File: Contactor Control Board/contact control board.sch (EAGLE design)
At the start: 34 parts, among them Q1 MMBT2222A, Q2 MMBT2222A, Q3 MOSFET-NCHANNELBSS123LT1G, Q6 MOSFET-NCHANNELBSS123LT1G

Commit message: Fixed values for FETs and some resistors whcih were cut and paste errors.
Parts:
- Q3, Q6: value MOSFET-NCHANNELBSS123LT1G -> IRLML6344TRPBF
- R1, R13, R3, R5: value 470k -> 470
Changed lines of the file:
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@@
 <part name="R11" library="SparkFun-Resistors" deviceset="RESISTOR" device="0603-RES" value="12k"/>
 <part name="R12" library="SparkFun-Resistors" deviceset="RESISTOR" device="0603-RES" value="100k"/>
-<part name="R13" library="SparkFun-Resistors" deviceset="RESISTOR" device="0603-RES" value="470k"/>
+<part name="R13" library="SparkFun-Resistors" deviceset="RESISTOR" device="0603-RES" value="470"/>
 <part name="R2" library="SparkFun-Resistors" deviceset="RESISTOR" device="0603-RES" value="1k"/>
-<part name="R1" library="SparkFun-Resistors" deviceset="RESISTOR" device="0603-RES" value="470k"/>
-<part name="R3" library="SparkFun-Resistors" deviceset="RESISTOR" device="0603-RES" value="470k"/>
-<part name="R5" library="SparkFun-Resistors" deviceset="RESISTOR" device="0603-RES" value="470k"/>
+<part name="R1" library="SparkFun-Resistors" deviceset="RESISTOR" device="0603-RES" value="470"/>
+<part name="R3" library="SparkFun-Resistors" deviceset="RESISTOR" device="0603-RES" value="470"/>
+<part name="R5" library="SparkFun-Resistors" deviceset="RESISTOR" device="0603-RES" value="470"/>
 <part name="R4" library="SparkFun-Resistors" deviceset="RESISTOR" device="0603-RES" value="10k"/>
 <part name="R6" library="SparkFun-Resistors" deviceset="RESISTOR" device="0603-RES" value="10k"/>
@@
 <part name="Q2" library="SparkFun-DiscreteSemi" deviceset="TRANSISTOR_NPN" device="MMBT2222A" value="MMBT2222A"/>
 <part name="Q1" library="SparkFun-DiscreteSemi" deviceset="TRANSISTOR_NPN" device="MMBT2222A" value="MMBT2222A"/>
-<part name="Q3" library="SparkFun-DiscreteSemi" deviceset="MOSFET-NCHANNEL" device="BSS123LT1G"/>
-<part name="Q6" library="SparkFun-DiscreteSemi" deviceset="MOSFET-NCHANNEL" device="BSS123LT1G"/>
+<part name="Q3" library="SparkFun-DiscreteSemi" deviceset="MOSFET-NCHANNEL" device="BSS123LT1G" value="IRLML6344TRPBF"/>
+<part name="Q6" library="SparkFun-DiscreteSemi" deviceset="MOSFET-NCHANNEL" device="BSS123LT1G" value="IRLML6344TRPBF"/>
 <part name="LM393M" library="Fairchild_By_element14_Batch_1" deviceset="LM393M" device=""/>
 <part name="74HC125M" library="Fairchild_By_element14_Batch_1" deviceset="MM74HC125M" device=""/>

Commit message: Fixed wiring of capacitor charge sensing which caused ground planes to need re-routing
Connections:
- net CAP_CHARGE_REF: now also LM393M.IN1_(-); no longer LM393M.IN1_(+)
- net CAP_CHARGE_V_CURR: now also LM393M.IN1_(+); no longer LM393M.IN1_(-)
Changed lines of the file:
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@@
 </segment>
 <segment>
-<wire x1="114.3" y1="121.92" x2="104.14" y2="121.92" width="0.2032" layer="91"/>
-<label x="104.14" y="121.92" size="1.778" layer="95" rot="R180"/>
-<pinref part="LM393M" gate="A" pin="IN1_(+)"/>
+<wire x1="114.3" y1="119.38" x2="104.14" y2="119.38" width="0.2032" layer="91"/>
+<label x="104.14" y="119.38" size="1.778" layer="95" rot="R180"/>
+<pinref part="LM393M" gate="A" pin="IN1_(-)"/>
 </segment>
 </net>
@@
 </segment>
 <segment>
-<wire x1="114.3" y1="119.38" x2="104.14" y2="119.38" width="0.2032" layer="91"/>
-<label x="104.14" y="119.38" size="1.778" layer="95" rot="R180"/>
-<pinref part="LM393M" gate="A" pin="IN1_(-)"/>
+<wire x1="114.3" y1="121.92" x2="104.14" y2="121.92" width="0.2032" layer="91"/>
+<label x="104.14" y="121.92" size="1.778" layer="95" rot="R180"/>
+<pinref part="LM393M" gate="A" pin="IN1_(+)"/>
 </segment>
 </net>

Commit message: Finally found part # for fuse holder!
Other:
- note added: "Part #1A3399-10 from Mouser. Must order in multiples of 2"
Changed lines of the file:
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@@
 <text x="147.32" y="114.3" size="1.778" layer="95">*Output goes HIGH (5V) when cap charge goes
 ABOVE reference</text>
+<text x="-33.02" y="86.36" size="1.778" layer="95">Part #1A3399-10 from Mouser.
+Must order in multiples of 2</text>
 </plain>
 <instances>

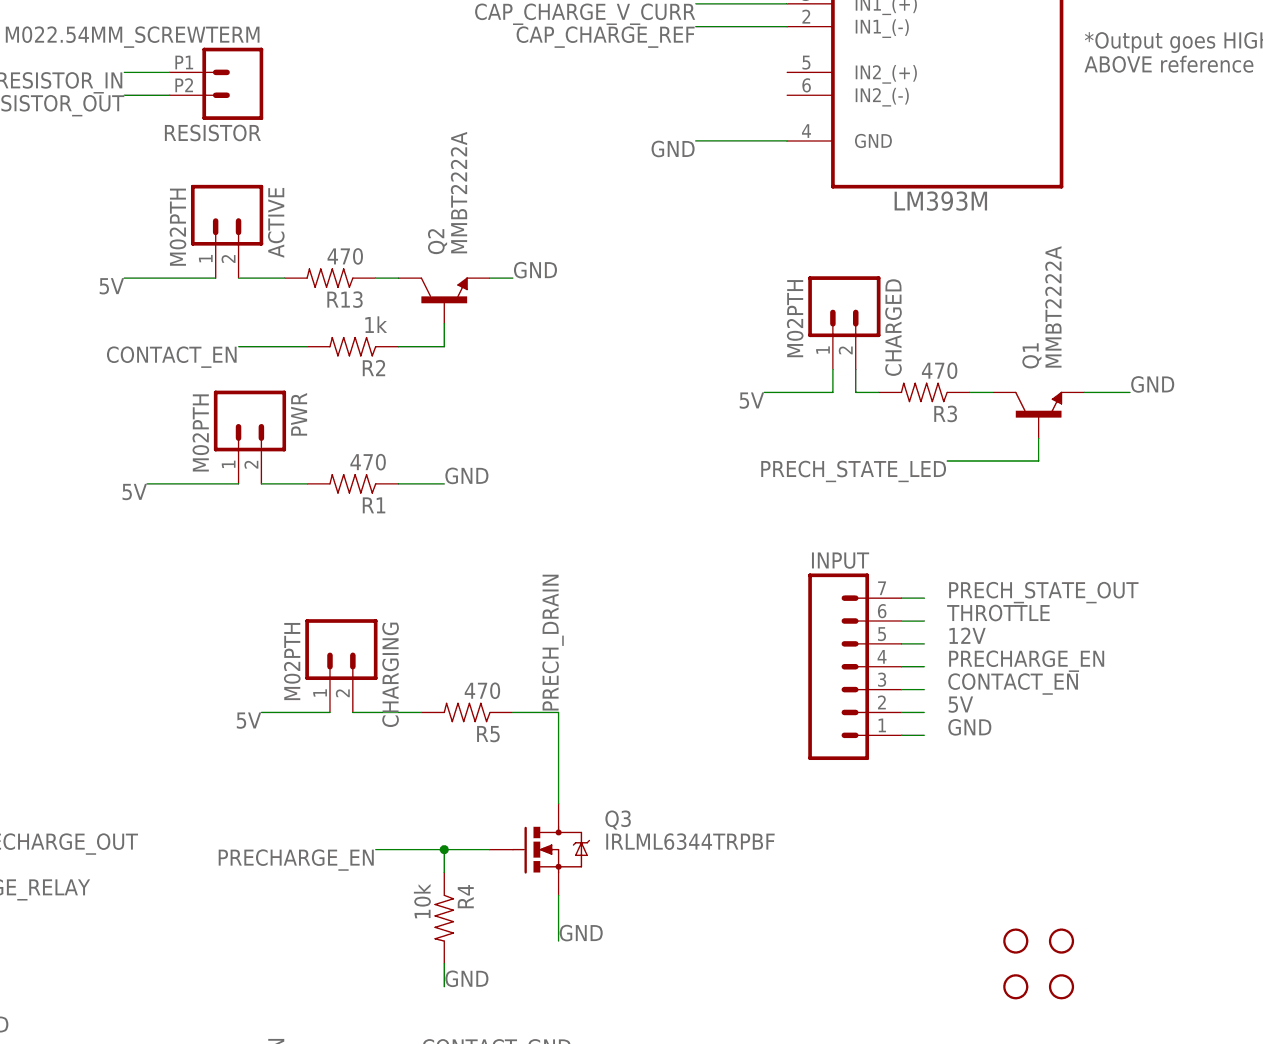
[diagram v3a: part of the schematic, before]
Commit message: CHanged all connectors on MCB to use Molex
Changed most of the connectors on the BMS interface to use molex as
well.
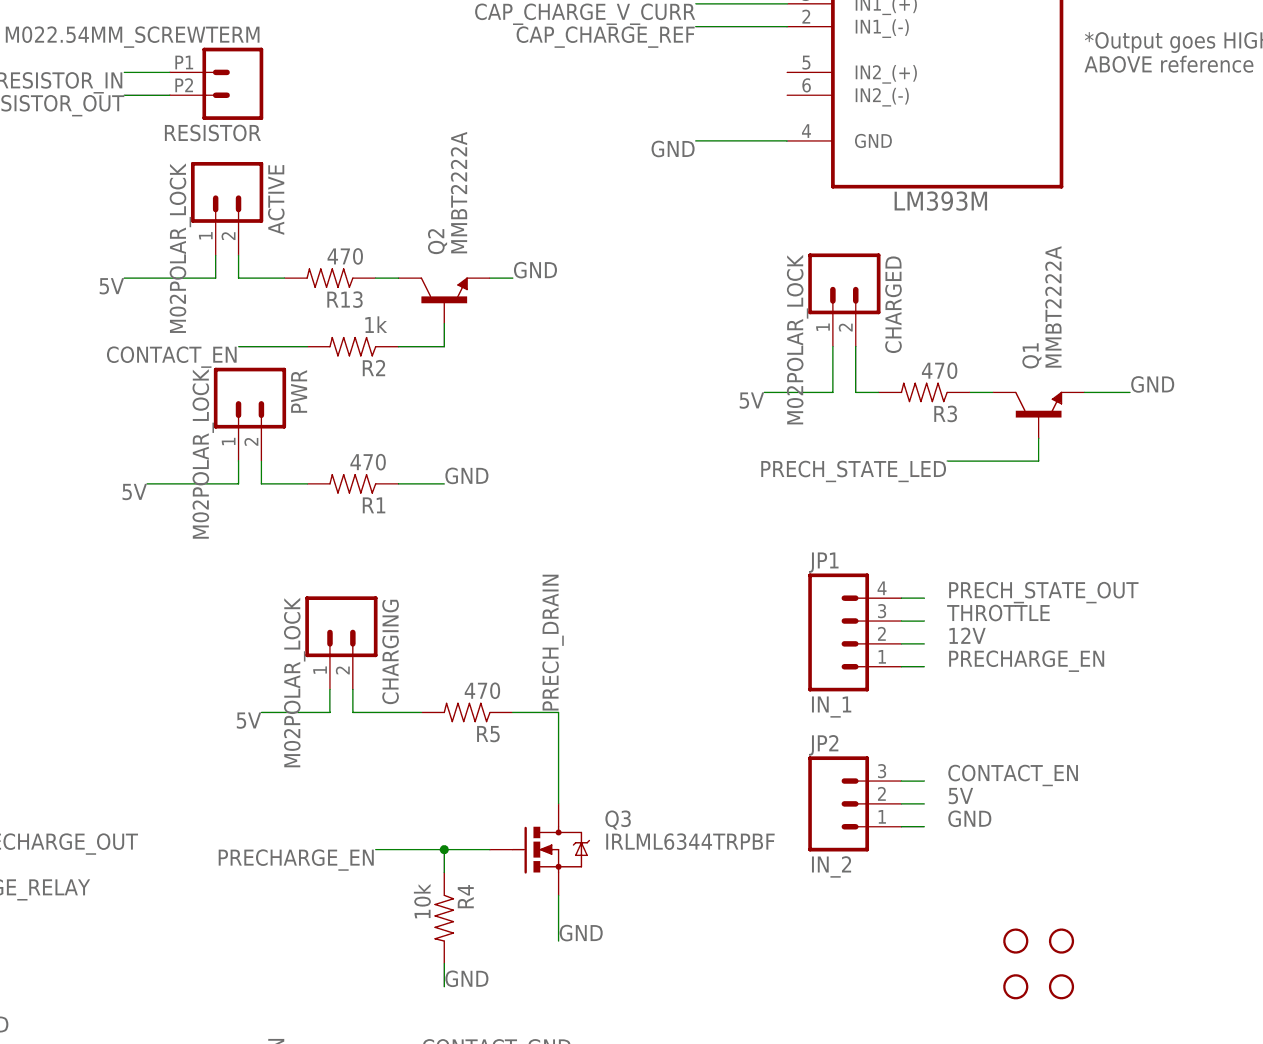
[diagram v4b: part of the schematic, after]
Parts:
- removed INPUT: (no value), SparkFun-Connectors:M07
- added JP1: IN_1, SparkFun-Connectors:M04POLAR_LOCK
- added JP2: IN_2, SparkFun-Connectors:M03POLAR_LOCK
- ACTIVE, CHARGED, CHARGING, PWR: value M02PTH -> M02POLAR_LOCK; device SparkFun-Connectors:M02PTH -> SparkFun-Connectors:M02POLAR_LOCK
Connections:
- net 12V: now also JP1.2; no longer INPUT.5
- net 5V: now also JP2.2; no longer INPUT.2
- net CONTACT_EN: now also JP2.3; no longer INPUT.3
- net GND: now also JP2.1; no longer INPUT.1
- net PRECHARGE_EN: now also JP1.1; no longer INPUT.4
- net PRECH_STATE_OUT: now also JP1.4; no longer INPUT.7
- net THROTTLE: now also JP1.3; no longer INPUT.6
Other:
- moved on the sheet: ACTIVE, CHARGED, CHARGING, PWR
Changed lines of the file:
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@@
 <part name="STANDOFF4" library="SparkFun-Electromechanical" deviceset="STAND-OFF" device=""/>
 <part name="PRECHARGE_FUSE" library="SparkFun-Passives" deviceset="FUSE" device="X20MM"/>
-<part name="ACTIVE" library="SparkFun-Connectors" deviceset="M02" device="PTH"/>
-<part name="PWR" library="SparkFun-Connectors" deviceset="M02" device="PTH"/>
-<part name="CHARGING" library="SparkFun-Connectors" deviceset="M02" device="PTH"/>
 <part name="RESISTOR" library="SparkFun-Connectors" deviceset="M02" device="2.54MM_SCREWTERM"/>
 <part name="PRECHARGE_RELAY" library="relay" deviceset="DS2Y-S-DC*" device="" technology="5V"/>
-<part name="INPUT" library="SparkFun-Connectors" deviceset="M07" device=""/>
-<part name="CHARGED" library="SparkFun-Connectors" deviceset="M02" device="PTH"/>
 <part name="R14" library="SparkFun-Resistors" deviceset="RESISTOR" device="0603-RES" value="470k"/>
 <part name="R8" library="SparkFun-Resistors" deviceset="RESISTOR" device="0603-RES" value="13k"/>
@@
 <part name="LM393M" library="Fairchild_By_element14_Batch_1" deviceset="LM393M" device=""/>
 <part name="74HC125M" library="Fairchild_By_element14_Batch_1" deviceset="MM74HC125M" device=""/>
+<part name="JP1" library="SparkFun-Connectors" deviceset="M04" device="POLAR_LOCK" value="IN_1"/>
+<part name="JP2" library="SparkFun-Connectors" deviceset="M03" device="POLAR_LOCK" value="IN_2"/>
+<part name="CHARGING" library="SparkFun-Connectors" deviceset="M02" device="POLAR_LOCK"/>
+<part name="PWR" library="SparkFun-Connectors" deviceset="M02" device="POLAR_LOCK"/>
+<part name="ACTIVE" library="SparkFun-Connectors" deviceset="M02" device="POLAR_LOCK"/>
+<part name="CHARGED" library="SparkFun-Connectors" deviceset="M02" device="POLAR_LOCK"/>
 </parts>
 <sheets>
@@
 <instance part="STANDOFF4" gate="G$1" x="139.7" y="12.7"/>
 <instance part="PRECHARGE_FUSE" gate="G$1" x="-15.24" y="78.74" rot="R180"/>
-<instance part="ACTIVE" gate="G$1" x="50.8" y="99.06" rot="R270"/>
-<instance part="PWR" gate="G$1" x="53.34" y="76.2" rot="R270"/>
-<instance part="CHARGING" gate="G$1" x="63.5" y="50.8" rot="R270"/>
 <instance part="RESISTOR" gate="G$1" x="53.34" y="114.3" rot="R180"/>
 <instance part="PRECHARGE_RELAY" gate="1" x="-40.64" y="12.7"/>
 <instance part="PRECHARGE_RELAY" gate="2" x="12.7" y="22.86"/>
 <instance part="PRECHARGE_RELAY" gate="3" x="12.7" y="2.54"/>
-<instance part="INPUT" gate="G$1" x="121.92" y="45.72"/>
-<instance part="CHARGED" gate="G$1" x="119.38" y="88.9" rot="R270"/>
 <instance part="R14" gate="G$1" x="71.12" y="160.02" rot="R90"/>
 <instance part="R8" gate="G$1" x="71.12" y="147.32" rot="R90"/>
@@
 <instance part="LM393M" gate="A" x="132.08" y="119.38"/>
 <instance part="74HC125M" gate="A" x="241.3" y="93.98"/>
+<instance part="JP1" gate="G$1" x="121.92" y="50.8"/>
+<instance part="JP2" gate="G$1" x="119.38" y="33.02"/>
+<instance part="CHARGING" gate="G$1" x="63.5" y="53.34" rot="R270"/>
+<instance part="PWR" gate="G$1" x="53.34" y="78.74" rot="R270"/>
+<instance part="ACTIVE" gate="G$1" x="50.8" y="101.6" rot="R270"/>
+<instance part="CHARGED" gate="G$1" x="119.38" y="91.44" rot="R270"/>
 </instances>
 <busses>
@@
 <net name="5V" class="0">
 <segment>
-<wire x1="127" y1="43.18" x2="129.54" y2="43.18" width="0.2032" layer="91"/>
-<label x="132.08" y="43.18" size="1.778" layer="95"/>
-<pinref part="INPUT" gate="G$1" pin="2"/>
-</segment>
-<segment>
 <wire x1="40.64" y1="91.44" x2="50.8" y2="91.44" width="0.2032" layer="91"/>
+<label x="40.64" y="91.44" size="1.778" layer="95" rot="R180"/>
 <pinref part="ACTIVE" gate="G$1" pin="1"/>
-<label x="40.64" y="91.44" size="1.778" layer="95" rot="R180"/>
-</segment>
-<segment>
-<pinref part="PWR" gate="G$1" pin="1"/>
+<wire x1="50.8" y1="93.98" x2="50.8" y2="91.44" width="0.2032" layer="91"/>
+</segment>
+<segment>
 <wire x1="53.34" y1="68.58" x2="43.18" y2="68.58" width="0.2032" layer="91"/>
 <label x="43.18" y="68.58" size="1.778" layer="95" rot="R180"/>
+<pinref part="PWR" gate="G$1" pin="1"/>
+<wire x1="53.34" y1="71.12" x2="53.34" y2="68.58" width="0.2032" layer="91"/>
 </segment>
 <segment>
@@
 </segment>
 <segment>
-<pinref part="CHARGED" gate="G$1" pin="1"/>
-<wire x1="119.38" y1="81.28" x2="119.38" y2="78.74" width="0.2032" layer="91"/>
 <wire x1="119.38" y1="78.74" x2="111.76" y2="78.74" width="0.2032" layer="91"/>
 <label x="111.76" y="78.74" size="1.778" layer="95" rot="R180"/>
+<pinref part="CHARGED" gate="G$1" pin="1"/>
+<wire x1="119.38" y1="83.82" x2="119.38" y2="78.74" width="0.2032" layer="91"/>
 </segment>
 <segment>
@@
 </segment>
 <segment>
-<pinref part="CHARGING" gate="G$1" pin="1"/>
 <wire x1="63.5" y1="43.18" x2="55.88" y2="43.18" width="0.2032" layer="91"/>
 <label x="55.88" y="43.18" size="1.778" layer="95" rot="R180"/>
+<pinref part="CHARGING" gate="G$1" pin="1"/>
+<wire x1="63.5" y1="45.72" x2="63.5" y2="43.18" width="0.2032" layer="91"/>
+</segment>
+<segment>
+<pinref part="JP2" gate="G$1" pin="2"/>
+<wire x1="127" y1="33.02" x2="129.54" y2="33.02" width="0.2032" layer="91"/>
+<label x="132.08" y="33.02" size="1.778" layer="95"/>
 </segment>
 </net>
@@
 <label x="58.42" y="-22.86" size="1.778" layer="95"/>
 <pinref part="R6" gate="G$1" pin="2"/>
-</segment>
-<segment>
-<wire x1="127" y1="40.64" x2="129.54" y2="40.64" width="0.2032" layer="91"/>
-<label x="132.08" y="40.64" size="1.778" layer="95"/>
-<pinref part="INPUT" gate="G$1" pin="1"/>
 </segment>
 <segment>
@@
 <label x="218.44" y="76.2" size="1.778" layer="95" rot="R180"/>
 </segment>
+<segment>
+<pinref part="JP2" gate="G$1" pin="1"/>
+<wire x1="127" y1="30.48" x2="129.54" y2="30.48" width="0.2032" layer="91"/>
+<label x="132.08" y="30.48" size="1.778" layer="95"/>
+</segment>
 </net>
 <net name="CONTACT_EN" class="0">
-<segment>
-<wire x1="127" y1="45.72" x2="129.54" y2="45.72" width="0.2032" layer="91"/>
-<label x="132.08" y="45.72" size="1.778" layer="95"/>
-<pinref part="INPUT" gate="G$1" pin="3"/>
-</segment>
 <segment>
 <wire x1="66.04" y1="-5.08" x2="58.42" y2="-5.08" width="0.2032" layer="91"/>
@@
 <pinref part="R2" gate="G$1" pin="2"/>
 </segment>
+<segment>
+<pinref part="JP2" gate="G$1" pin="3"/>
+<wire x1="127" y1="35.56" x2="129.54" y2="35.56" width="0.2032" layer="91"/>
+<label x="132.08" y="35.56" size="1.778" layer="95"/>
+</segment>
 </net>
 <net name="PRECHARGE_EN" class="0">
@@
 <wire x1="127" y1="48.26" x2="129.54" y2="48.26" width="0.2032" layer="91"/>
 <label x="132.08" y="48.26" size="1.778" layer="95"/>
-<pinref part="INPUT" gate="G$1" pin="4"/>
+<pinref part="JP1" gate="G$1" pin="1"/>
 </segment>
 <segment>
@@
 <wire x1="127" y1="50.8" x2="129.54" y2="50.8" width="0.2032" layer="91"/>
 <label x="132.08" y="50.8" size="1.778" layer="95"/>
-<pinref part="INPUT" gate="G$1" pin="5"/>
+<pinref part="JP1" gate="G$1" pin="2"/>
 </segment>
 <segment>
@@
 <wire x1="127" y1="53.34" x2="129.54" y2="53.34" width="0.2032" layer="91"/>
 <label x="132.08" y="53.34" size="1.778" layer="95"/>
-<pinref part="INPUT" gate="G$1" pin="6"/>
+<pinref part="JP1" gate="G$1" pin="3"/>
 </segment>
 <segment>
@@
 <net name="N$9" class="0">
 <segment>
-<pinref part="ACTIVE" gate="G$1" pin="2"/>
 <wire x1="53.34" y1="91.44" x2="58.42" y2="91.44" width="0.2032" layer="91"/>
 <pinref part="R13" gate="G$1" pin="2"/>
+<pinref part="ACTIVE" gate="G$1" pin="2"/>
+<wire x1="53.34" y1="93.98" x2="53.34" y2="91.44" width="0.2032" layer="91"/>
 </segment>
 </net>
 <net name="N$12" class="0">
 <segment>
-<pinref part="PWR" gate="G$1" pin="2"/>
 <wire x1="55.88" y1="68.58" x2="60.96" y2="68.58" width="0.2032" layer="91"/>
 <pinref part="R1" gate="G$1" pin="2"/>
+<pinref part="PWR" gate="G$1" pin="2"/>
+<wire x1="55.88" y1="71.12" x2="55.88" y2="68.58" width="0.2032" layer="91"/>
 </segment>
 </net>
@@
 <wire x1="127" y1="55.88" x2="129.54" y2="55.88" width="0.2032" layer="91"/>
 <label x="132.08" y="55.88" size="1.778" layer="95"/>
-<pinref part="INPUT" gate="G$1" pin="7"/>
+<pinref part="JP1" gate="G$1" pin="4"/>
 </segment>
 <segment>
@@
 <net name="N$4" class="0">
 <segment>
-<pinref part="CHARGED" gate="G$1" pin="2"/>
-<wire x1="121.92" y1="81.28" x2="121.92" y2="78.74" width="0.2032" layer="91"/>
 <wire x1="121.92" y1="78.74" x2="124.46" y2="78.74" width="0.2032" layer="91"/>
 <pinref part="R3" gate="G$1" pin="2"/>
+<pinref part="CHARGED" gate="G$1" pin="2"/>
+<wire x1="121.92" y1="83.82" x2="121.92" y2="78.74" width="0.2032" layer="91"/>
 </segment>
 </net>
@@
 <net name="N$7" class="0">
 <segment>
-<pinref part="CHARGING" gate="G$1" pin="2"/>
 <wire x1="66.04" y1="43.18" x2="73.66" y2="43.18" width="0.2032" layer="91"/>
 <pinref part="R5" gate="G$1" pin="2"/>
-</segment>
-</net>
+<pinref part="CHARGING" gate="G$1" pin="2"/>
+<wire x1="66.04" y1="45.72" x2="66.04" y2="43.18" width="0.2032" layer="91"/>
+</segment>
+</net>
